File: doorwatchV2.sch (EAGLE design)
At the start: 40 parts, among them IC2 MAX3232CPE, K1 FINDER-43.61, Q1 IRLZ44Z, T1 BC847, T2 BC847, T3 BC847, T4 BC847, X1 MKDSN1,5/2-5,08, X2 D-SUB9-H2M09RA, X3 MKDSN1,5/2-5,08

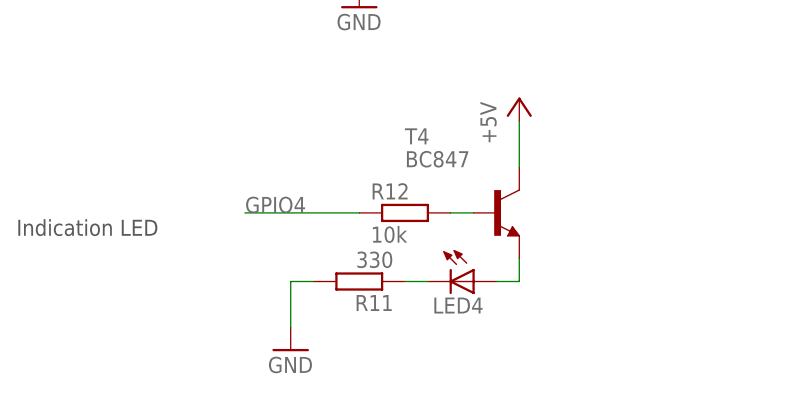
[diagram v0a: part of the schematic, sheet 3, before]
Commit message: first rough layout of components
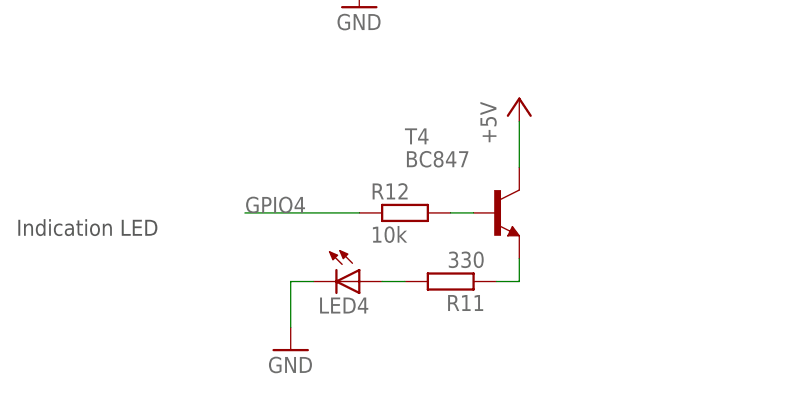
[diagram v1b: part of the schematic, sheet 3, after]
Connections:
- net GND: now also LED4.C; no longer R11.2
- net N$28: now also R11.1; no longer LED4.A
- net N$29: now also LED4.A, R11.2; no longer LED4.C, R11.1
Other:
- moved on the sheet: LED4, R11
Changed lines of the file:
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@@
 <instance part="T3" gate="G$1" x="-15.24" y="2.54"/>
 <instance part="R10" gate="G$1" x="-20.32" y="-20.32"/>
-<instance part="LED4" gate="G$1" x="-53.34" y="-99.06" rot="R270"/>
-<instance part="R11" gate="G$1" x="-66.04" y="-99.06" rot="R180"/>
+<instance part="LED4" gate="G$1" x="-66.04" y="-99.06" rot="R270"/>
+<instance part="R11" gate="G$1" x="-55.88" y="-99.06" rot="R180"/>
 <instance part="T4" gate="G$1" x="-50.8" y="-91.44"/>
 <instance part="R12" gate="G$1" x="-60.96" y="-91.44"/>
@@
 </segment>
 <segment>
-<pinref part="R11" gate="G$1" pin="2"/>
-<wire x1="-71.12" y1="-99.06" x2="-73.66" y2="-99.06" width="0.1524" layer="91"/>
 <wire x1="-73.66" y1="-99.06" x2="-73.66" y2="-104.14" width="0.1524" layer="91"/>
 <pinref part="GND5" gate="1" pin="GND"/>
+<pinref part="LED4" gate="G$1" pin="C"/>
+<wire x1="-73.66" y1="-99.06" x2="-71.12" y2="-99.06" width="0.1524" layer="91"/>
 </segment>
 </net>
@@
 <segment>
 <pinref part="T4" gate="G$1" pin="E"/>
+<wire x1="-48.26" y1="-96.52" x2="-48.26" y2="-99.06" width="0.1524" layer="91"/>
+<pinref part="R11" gate="G$1" pin="1"/>
+<wire x1="-50.8" y1="-99.06" x2="-48.26" y2="-99.06" width="0.1524" layer="91"/>
+</segment>
+</net>
+<net name="N$29" class="0">
+<segment>
 <pinref part="LED4" gate="G$1" pin="A"/>
-<wire x1="-48.26" y1="-96.52" x2="-48.26" y2="-99.06" width="0.1524" layer="91"/>
-<wire x1="-48.26" y1="-99.06" x2="-50.8" y2="-99.06" width="0.1524" layer="91"/>
-</segment>
-</net>
-<net name="N$29" class="0">
-<segment>
-<pinref part="LED4" gate="G$1" pin="C"/>
-<pinref part="R11" gate="G$1" pin="1"/>
-<wire x1="-58.42" y1="-99.06" x2="-60.96" y2="-99.06" width="0.1524" layer="91"/>
-</segment>
-</net>
+<pinref part="R11" gate="G$1" pin="2"/>
+<wire x1="-63.5" y1="-99.06" x2="-60.96" y2="-99.06" width="0.1524" layer="91"/>
+</segment>
+</net>

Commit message: added mounting-holes to schematic
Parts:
- added H1, H2, H3, H4: MOUNT-HOLE3.2, holes:MOUNT-HOLE3.2
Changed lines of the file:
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@@
 <part name="P+8" library="supply1" deviceset="+5V" device=""/>
 <part name="GND5" library="supply1" deviceset="GND" device=""/>
+<part name="H1" library="holes" deviceset="MOUNT-HOLE" device="3.2"/>
+<part name="H2" library="holes" deviceset="MOUNT-HOLE" device="3.2"/>
+<part name="H3" library="holes" deviceset="MOUNT-HOLE" device="3.2"/>
+<part name="H4" library="holes" deviceset="MOUNT-HOLE" device="3.2"/>
 </parts>
 <sheets>
@@
 </nets>
 </sheet>
+<sheet>
+<description>Drills</description>
+<plain>
+</plain>
+<instances>
+<instance part="H1" gate="G$1" x="17.78" y="81.28"/>
+<instance part="H2" gate="G$1" x="17.78" y="73.66"/>
+<instance part="H3" gate="G$1" x="17.78" y="66.04"/>
+<instance part="H4" gate="G$1" x="17.78" y="58.42"/>
+</instances>
+<busses>
+</busses>
+<nets>
+</nets>
+</sheet>

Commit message: first version of finished layout added white-print layers and adjusted it. adapted the trace width of higher current traces
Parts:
- removed H4: MOUNT-HOLE3.2, holes:MOUNT-HOLE3.2
- IC1: value (none) -> LM2576S-5.0
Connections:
- net +5V: now also R6.1; no longer LED3.A
- net GND: now also LED3.C; no longer R6.2
- net N$18: now also LED3.A, R6.2; no longer LED3.C, R6.1
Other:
- moved on the sheet: LED3, R6
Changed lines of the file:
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@@
 </classes>
 <parts>
-<part name="IC1" library="regulators" deviceset="LM2576" device="S"/>
+<part name="IC1" library="regulators" deviceset="LM2576" device="S" value="LM2576S-5.0"/>
 <part name="GND1" library="supply1" deviceset="GND" device=""/>
 <part name="L1" library="inductors" deviceset="DR125" device="" value="100uH"/>
@@
 <part name="H2" library="holes" deviceset="MOUNT-HOLE" device="3.2"/>
 <part name="H3" library="holes" deviceset="MOUNT-HOLE" device="3.2"/>
-<part name="H4" library="holes" deviceset="MOUNT-HOLE" device="3.2"/>
 </parts>
 <sheets>
@@
 <instance part="D3" gate="G$1" x="-66.04" y="-10.16" rot="R180"/>
 <instance part="P+4" gate="1" x="-53.34" y="10.16"/>
-<instance part="LED3" gate="G$1" x="58.42" y="0"/>
-<instance part="R6" gate="G$1" x="58.42" y="-12.7" rot="R270"/>
+<instance part="LED3" gate="G$1" x="58.42" y="-12.7"/>
+<instance part="R6" gate="G$1" x="58.42" y="-2.54" rot="R270"/>
 </instances>
 <busses>
@@
 <pinref part="D3" gate="G$1" pin="A"/>
 <wire x1="-63.5" y1="-10.16" x2="-53.34" y2="-10.16" width="0.1524" layer="91"/>
-<pinref part="R6" gate="G$1" pin="2"/>
-<wire x1="58.42" y1="-17.78" x2="58.42" y2="-20.32" width="0.1524" layer="91"/>
 <wire x1="58.42" y1="-20.32" x2="45.72" y2="-20.32" width="0.1524" layer="91"/>
 <junction x="45.72" y="-20.32"/>
+<pinref part="LED3" gate="G$1" pin="C"/>
+<wire x1="58.42" y1="-17.78" x2="58.42" y2="-20.32" width="0.1524" layer="91"/>
 </segment>
 </net>
@@
 <pinref part="P+1" gate="1" pin="+5V"/>
 <wire x1="58.42" y1="5.08" x2="58.42" y2="10.16" width="0.1524" layer="91"/>
-<pinref part="LED3" gate="G$1" pin="A"/>
-<wire x1="58.42" y1="2.54" x2="58.42" y2="5.08" width="0.1524" layer="91"/>
+<pinref part="R6" gate="G$1" pin="1"/>
+<wire x1="58.42" y1="5.08" x2="58.42" y2="2.54" width="0.1524" layer="91"/>
 <junction x="58.42" y="5.08"/>
 </segment>
@@
 <net name="N$18" class="0">
 <segment>
-<pinref part="LED3" gate="G$1" pin="C"/>
-<pinref part="R6" gate="G$1" pin="1"/>
-<wire x1="58.42" y1="-5.08" x2="58.42" y2="-7.62" width="0.1524" layer="91"/>
+<pinref part="R6" gate="G$1" pin="2"/>
+<pinref part="LED3" gate="G$1" pin="A"/>
+<wire x1="58.42" y1="-7.62" x2="58.42" y2="-10.16" width="0.1524" layer="91"/>
 </segment>
 </net>
@@
 <instance part="H2" gate="G$1" x="17.78" y="73.66"/>
 <instance part="H3" gate="G$1" x="17.78" y="66.04"/>
-<instance part="H4" gate="G$1" x="17.78" y="58.42"/>
 </instances>
 <busses>
@@
 </sheet>
 </sheets>
+<errors>
+</errors>
 </schematic>
 </drawing>

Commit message: added some text components to board to sign connectors
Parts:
- R12, R3, R7: value 10k -> 1k
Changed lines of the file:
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@@
 <part name="LED1" library="led" deviceset="LED" device="CHIP-LED0805"/>
 <part name="LED2" library="led" deviceset="LED" device="CHIP-LED0805"/>
-<part name="R3" library="rcl" deviceset="R-EU_" device="M0805" value="10k"/>
+<part name="R3" library="rcl" deviceset="R-EU_" device="M0805" value="1k"/>
 <part name="R4" library="rcl" deviceset="R-EU_" device="M0805" value="330"/>
 <part name="Q1" library="transistor-power" deviceset="IRLZ44Z" device=""/>
@@
 <part name="R6" library="rcl" deviceset="R-EU_" device="M0805" value="330"/>
 <part name="K1" library="relay" deviceset="FINDER-43.61" device=""/>
-<part name="R7" library="rcl" deviceset="R-EU_" device="M0805" value="10k"/>
+<part name="R7" library="rcl" deviceset="R-EU_" device="M0805" value="1k"/>
 <part name="P+7" library="supply1" deviceset="+12V" device=""/>
 <part name="X3" library="con-phoenix-508" deviceset="MKDSN1,5/2-5,08" device=""/>
@@
 <part name="R11" library="rcl" deviceset="R-EU_" device="M0805" value="330"/>
 <part name="T4" library="transistor" deviceset="BC847" device=""/>
-<part name="R12" library="rcl" deviceset="R-EU_" device="M0805" value="10k"/>
+<part name="R12" library="rcl" deviceset="R-EU_" device="M0805" value="1k"/>
 <part name="P+8" library="supply1" deviceset="+5V" device=""/>
 <part name="GND5" library="supply1" deviceset="GND" device=""/>

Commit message: changed C1 condensator to an elko type
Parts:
- C1: device rcl:C-EUC0805 -> rcl:CPOL-EUE2.5-7
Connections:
- net +12V: now also C1.+; no longer C1.1
- net GND: now also C1.-; no longer C1.2
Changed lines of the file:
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@@
 <?xml version="1.0" encoding="utf-8"?>
 <!DOCTYPE eagle SYSTEM "eagle.dtd">
-<eagle version="6.0">
+<eagle version="7.3.0">
 <drawing>
 <settings>
@@
 <grid distance="0.1" unitdist="inch" unit="inch" style="lines" multiple="1" display="no" altdistance="0.01" altunitdist="inch" altunit="inch"/>
 <layers>
-<layer number="1" name="Top" color="4" fill="1" visible="no" active="no"/>
-<layer number="2" name="Route2" color="1" fill="3" visible="no" active="no"/>
-<layer number="3" name="Route3" color="4" fill="3" visible="no" active="no"/>
-<layer number="4" name="Route4" color="1" fill="4" visible="no" active="no"/>
-<layer number="5" name="Route5" color="4" fill="4" visible="no" active="no"/>
-<layer number="6" name="Route6" color="1" fill="8" visible="no" active="no"/>
-<layer number="7" name="Route7" color="4" fill="8" visible="no" active="no"/>
-<layer number="8" name="Route8" color="1" fill="2" visible="no" active="no"/>
-<layer number="9" name="Route9" color="4" fill="2" visible="no" active="no"/>
-<layer number="10" name="Route10" color="1" fill="7" visible="no" active="no"/>
-<layer number="11" name="Route11" color="4" fill="7" visible="no" active="no"/>
-<layer number="12" name="Route12" color="1" fill="5" visible="no" active="no"/>
-<layer number="13" name="Route13" color="4" fill="5" visible="no" active="no"/>
-<layer number="14" name="Route14" color="1" fill="6" visible="no" active="no"/>
-<layer number="15" name="Route15" color="4" fill="6" visible="no" active="no"/>
-<layer number="16" name="Bottom" color="1" fill="1" visible="no" active="no"/>
-<layer number="17" name="Pads" color="2" fill="1" visible="no" active="no"/>
-<layer number="18" name="Vias" color="2" fill="1" visible="no" active="no"/>
-<layer number="19" name="Unrouted" color="6" fill="1" visible="no" active="no"/>
-<layer number="20" name="Dimension" color="15" fill="1" visible="no" active="no"/>
-<layer number="21" name="tPlace" color="7" fill="1" visible="no" active="no"/>
-<layer number="22" name="bPlace" color="7" fill="1" visible="no" active="no"/>
-<layer number="23" name="tOrigins" color="15" fill="1" visible="no" active="no"/>
-<layer number="24" name="bOrigins" color="15" fill="1" visible="no" active="no"/>
-<layer number="25" name="tNames" color="7" fill="1" visible="no" active="no"/>
-<layer number="26" name="bNames" color="7" fill="1" visible="no" active="no"/>
-<layer number="27" name="tValues" color="7" fill="1" visible="no" active="no"/>
-<layer number="28" name="bValues" color="7" fill="1" visible="no" active="no"/>
+<layer number="1" name="Top" color="4" fill="1" visible="yes" active="no"/>
+<layer number="2" name="Route2" color="1" fill="3" visible="yes" active="no"/>
+<layer number="3" name="Route3" color="4" fill="3" visible="yes" active="no"/>
+<layer number="4" name="Route4" color="1" fill="4" visible="yes" active="no"/>
+<layer number="5" name="Route5" color="4" fill="4" visible="yes" active="no"/>
+<layer number="6" name="Route6" color="1" fill="8" visible="yes" active="no"/>
+<layer number="7" name="Route7" color="4" fill="8" visible="yes" active="no"/>
+<layer number="8" name="Route8" color="1" fill="2" visible="yes" active="no"/>
+<layer number="9" name="Route9" color="4" fill="2" visible="yes" active="no"/>
+<layer number="10" name="Route10" color="1" fill="7" visible="yes" active="no"/>
+<layer number="11" name="Route11" color="4" fill="7" visible="yes" active="no"/>
+<layer number="12" name="Route12" color="1" fill="5" visible="yes" active="no"/>
+<layer number="13" name="Route13" color="4" fill="5" visible="yes" active="no"/>
+<layer number="14" name="Route14" color="1" fill="6" visible="yes" active="no"/>
+<layer number="15" name="Route15" color="4" fill="6" visible="yes" active="no"/>
+<layer number="16" name="Bottom" color="1" fill="1" visible="yes" active="no"/>
+<layer number="17" name="Pads" color="2" fill="1" visible="yes" active="no"/>
+<layer number="18" name="Vias" color="2" fill="1" visible="yes" active="no"/>
+<layer number="19" name="Unrouted" color="6" fill="1" visible="yes" active="no"/>
+<layer number="20" name="Dimension" color="15" fill="1" visible="yes" active="no"/>
+<layer number="21" name="tPlace" color="7" fill="1" visible="yes" active="no"/>
+<layer number="22" name="bPlace" color="7" fill="1" visible="yes" active="no"/>
+<layer number="23" name="tOrigins" color="15" fill="1" visible="yes" active="no"/>
+<layer number="24" name="bOrigins" color="15" fill="1" visible="yes" active="no"/>
+<layer number="25" name="tNames" color="7" fill="1" visible="yes" active="no"/>
+<layer number="26" name="bNames" color="7" fill="1" visible="yes" active="no"/>
+<layer number="27" name="tValues" color="7" fill="1" visible="yes" active="no"/>
+<layer number="28" name="bValues" color="7" fill="1" visible="yes" active="no"/>
 <layer number="29" name="tStop" color="7" fill="3" visible="no" active="no"/>
 <layer number="30" name="bStop" color="7" fill="6" visible="no" active="no"/>
@@
 <layer number="35" name="tGlue" color="7" fill="4" visible="no" active="no"/>
 <layer number="36" name="bGlue" color="7" fill="5" visible="no" active="no"/>
-<layer number="37" name="tTest" color="7" fill="1" visible="no" active="no"/>
-<layer number="38" name="bTest" color="7" fill="1" visible="no" active="no"/>
+<layer number="37" name="tTest" color="7" fill="1" visible="yes" active="no"/>
+<layer number="38" name="bTest" color="7" fill="1" visible="yes" active="no"/>
 <layer number="39" name="tKeepout" color="4" fill="11" visible="no" active="no"/>
 <layer number="40" name="bKeepout" color="1" fill="11" visible="no" active="no"/>
@@
 <layer number="44" name="Drills" color="7" fill="1" visible="no" active="no"/>
 <layer number="45" name="Holes" color="7" fill="1" visible="no" active="no"/>
-<layer number="46" name="Milling" color="3" fill="1" visible="no" active="no"/>
-<layer number="47" name="Measures" color="7" fill="1" visible="no" active="no"/>
-<layer number="48" name="Document" color="7" fill="1" visible="no" active="no"/>
-<layer number="49" name="Reference" color="7" fill="1" visible="no" active="no"/>
-<layer number="51" name="tDocu" color="7" fill="1" visible="no" active="no"/>
-<layer number="52" name="bDocu" color="7" fill="1" visible="no" active="no"/>
+<layer number="46" name="Milling" color="3" fill="1" visible="yes" active="no"/>
+<layer number="47" name="Measures" color="7" fill="1" visible="yes" active="no"/>
+<layer number="48" name="Document" color="7" fill="1" visible="yes" active="no"/>
+<layer number="49" name="Reference" color="7" fill="1" visible="yes" active="no"/>
+<layer number="51" name="tDocu" color="7" fill="1" visible="yes" active="no"/>
+<layer number="52" name="bDocu" color="7" fill="1" visible="yes" active="no"/>
 <layer number="91" name="Nets" color="2" fill="1" visible="yes" active="yes"/>
 <layer number="92" name="Busses" color="1" fill="1" visible="yes" active="yes"/>
@@
 <part name="L1" library="inductors" deviceset="DR125" device="" value="100uH"/>
 <part name="D1" library="diode" deviceset="1N581*" device="" technology="7-B"/>
-<part name="C1" library="rcl" deviceset="C-EU" device="C0805" value="100uF"/>
+<part name="C1" library="rcl" deviceset="CPOL-EU" device="E2.5-7" value="100uF"/>
 <part name="C2" library="rcl" deviceset="CPOL-EU" device="E5-10.5" value="1000uF"/>
 <part name="P+1" library="supply1" deviceset="+5V" device=""/>
@@
 <pinref part="C2" gate="G$1" pin="-"/>
 <wire x1="45.72" y1="-20.32" x2="45.72" y2="-15.24" width="0.1524" layer="91"/>
-<pinref part="C1" gate="G$1" pin="2"/>
+<pinref part="C1" gate="G$1" pin="-"/>
 <wire x1="-35.56" y1="-15.24" x2="-35.56" y2="-20.32" width="0.1524" layer="91"/>
 <wire x1="-35.56" y1="-20.32" x2="-20.32" y2="-20.32" width="0.1524" layer="91"/>
@@
 <pinref part="IC1" gate="G$1" pin="VIN"/>
 <wire x1="-17.78" y1="5.08" x2="-35.56" y2="5.08" width="0.1524" layer="91"/>
-<pinref part="C1" gate="G$1" pin="1"/>
+<pinref part="C1" gate="G$1" pin="+"/>
 <wire x1="-35.56" y1="5.08" x2="-53.34" y2="5.08" width="0.1524" layer="91"/>
 <wire x1="-35.56" y1="5.08" x2="-35.56" y2="-7.62" width="0.1524" layer="91"/>

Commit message: added reichelt.de warenkorb, package of inductive has been replaced, new routing of inductive and elko are necessary
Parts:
- L1: device inductors:DR125 -> rcl:L-EU0207/7
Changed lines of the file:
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@@
 <part name="IC1" library="regulators" deviceset="LM2576" device="S" value="LM2576S-5.0"/>
 <part name="GND1" library="supply1" deviceset="GND" device=""/>
-<part name="L1" library="inductors" deviceset="DR125" device="" value="100uH"/>
+<part name="L1" library="rcl" deviceset="L-EU" device="0207/7" value="100uH"/>
 <part name="D1" library="diode" deviceset="1N581*" device="" technology="7-B"/>
 <part name="C1" library="rcl" deviceset="CPOL-EU" device="E2.5-7" value="100uF"/>
@@
 <instance part="IC1" gate="G$1" x="0" y="0"/>
 <instance part="GND1" gate="1" x="0" y="-22.86"/>
-<instance part="L1" gate="G$1" x="33.02" y="-2.54"/>
+<instance part="L1" gate="G$1" x="33.02" y="-2.54" rot="R90"/>
 <instance part="D1" gate="G$1" x="22.86" y="-12.7" rot="R90"/>
 <instance part="C1" gate="G$1" x="-35.56" y="-10.16"/>
@@
 <segment>
 <pinref part="IC1" gate="G$1" pin="VO"/>
-<pinref part="L1" gate="G$1" pin="1"/>
 <wire x1="17.78" y1="-2.54" x2="22.86" y2="-2.54" width="0.1524" layer="91"/>
 <pinref part="D1" gate="G$1" pin="C"/>
-<wire x1="22.86" y1="-2.54" x2="25.4" y2="-2.54" width="0.1524" layer="91"/>
 <wire x1="22.86" y1="-10.16" x2="22.86" y2="-2.54" width="0.1524" layer="91"/>
+<pinref part="L1" gate="G$1" pin="1"/>
+<wire x1="22.86" y1="-2.54" x2="27.94" y2="-2.54" width="0.1524" layer="91"/>
 <junction x="22.86" y="-2.54"/>
 </segment>
@@
 <net name="+5V" class="0">
 <segment>
-<pinref part="L1" gate="G$1" pin="2"/>
-<wire x1="40.64" y1="-2.54" x2="45.72" y2="-2.54" width="0.1524" layer="91"/>
 <pinref part="IC1" gate="G$1" pin="FBACK"/>
 <wire x1="17.78" y1="5.08" x2="45.72" y2="5.08" width="0.1524" layer="91"/>
 <wire x1="45.72" y1="5.08" x2="45.72" y2="-2.54" width="0.1524" layer="91"/>
-<junction x="45.72" y="-2.54"/>
 <pinref part="C2" gate="G$1" pin="+"/>
-<wire x1="45.72" y1="-7.62" x2="45.72" y2="-2.54" width="0.1524" layer="91"/>
+<wire x1="45.72" y1="-2.54" x2="45.72" y2="-7.62" width="0.1524" layer="91"/>
 <wire x1="45.72" y1="5.08" x2="58.42" y2="5.08" width="0.1524" layer="91"/>
 <junction x="45.72" y="5.08"/>
@@
 <wire x1="58.42" y1="5.08" x2="58.42" y2="2.54" width="0.1524" layer="91"/>
 <junction x="58.42" y="5.08"/>
+<pinref part="L1" gate="G$1" pin="2"/>
+<wire x1="38.1" y1="-2.54" x2="45.72" y2="-2.54" width="0.1524" layer="91"/>
+<junction x="45.72" y="-2.54"/>
 </segment>
 </net>

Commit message: updated board
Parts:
- L1: device rcl:L-EU0207/7 -> rcl:L-EU0207/12
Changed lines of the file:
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@@
 <?xml version="1.0" encoding="utf-8"?>
 <!DOCTYPE eagle SYSTEM "eagle.dtd">
-<eagle version="7.3.0">
+<eagle version="6.0">
 <drawing>
 <settings>
@@
 <part name="IC1" library="regulators" deviceset="LM2576" device="S" value="LM2576S-5.0"/>
 <part name="GND1" library="supply1" deviceset="GND" device=""/>
-<part name="L1" library="rcl" deviceset="L-EU" device="0207/7" value="100uH"/>
+<part name="L1" library="rcl" deviceset="L-EU" device="0207/12" value="100uH"/>
 <part name="D1" library="diode" deviceset="1N581*" device="" technology="7-B"/>
 <part name="C1" library="rcl" deviceset="CPOL-EU" device="E2.5-7" value="100uF"/>

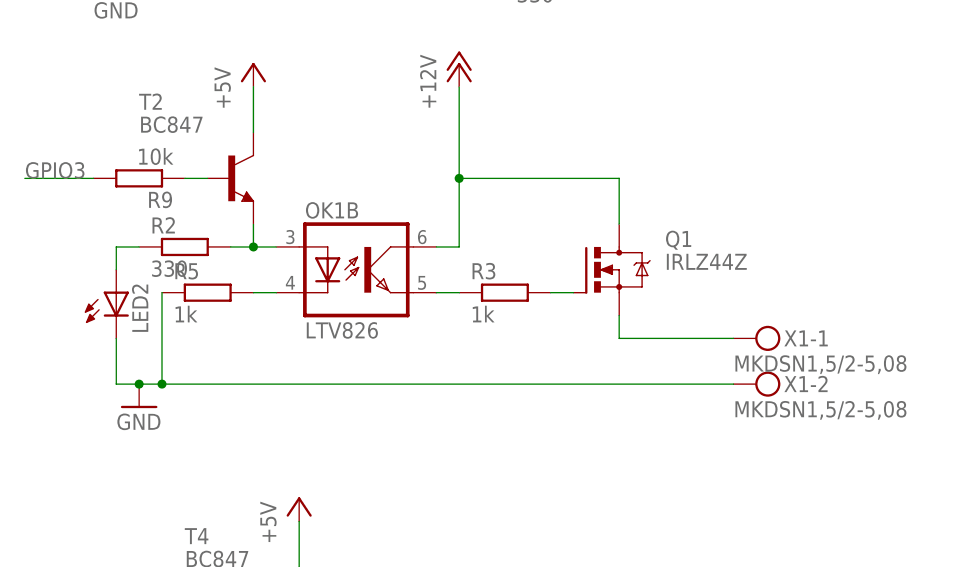
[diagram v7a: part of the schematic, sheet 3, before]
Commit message: fixed two bugs: 1) wrong polarity of power-jack 2) missing pull-down resistor on output of LTV826 opto-coupler, in front of MOSFET IRLZ44Z
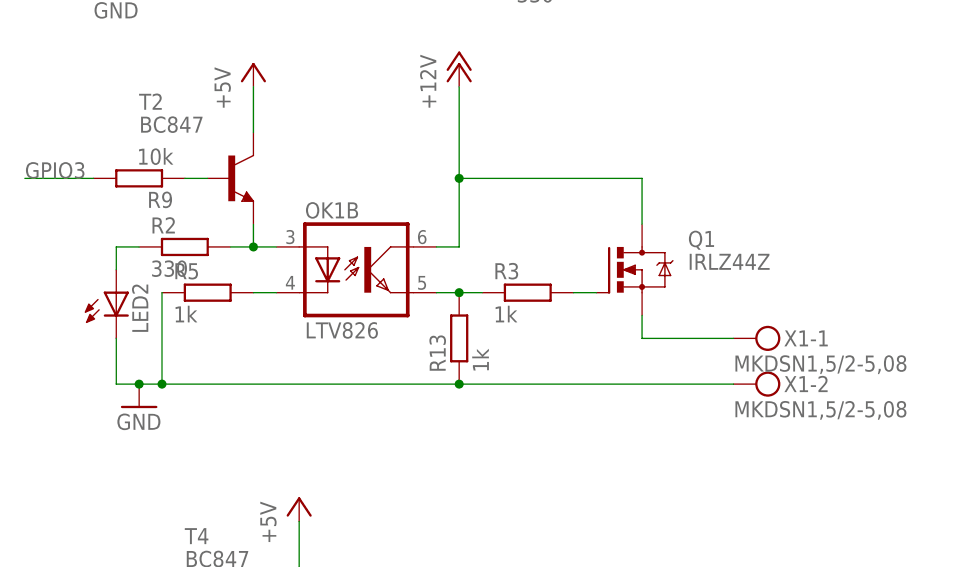
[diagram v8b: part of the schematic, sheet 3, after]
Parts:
- added R13: 1k, rcl:R-EU_M0805
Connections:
- net +12V: now also X4.1; no longer X4.3
- net GND: now also R13.1
- net N$15: now also X4.2, X4.3; no longer X4.1
- net N$16: now also R13.2
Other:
- moved on the sheet: Q1, R3, X4
